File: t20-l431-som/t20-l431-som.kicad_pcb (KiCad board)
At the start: 4 copper layers, 10.1 x 12.2 mm, 54 parts, among them U1 STM32L431-WLCSP64, U2 T20W80, U3 MX25U3232F, U4 MODULE_INTERNAL_T20_L431_HOST, U5 LP3986TL-2518/NOPB, U6 74LVC1T45_DSBGA_YZP, U7 TPS22916BYFPR, U8 SIT8021AI-J4-XXS-16.000000, U9 NCP139AFCT120T2G

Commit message: Various layout fixes for DRC
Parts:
- moved R7 0.20 mm to (89.2, 73.1)
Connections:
- U4 pad D11: (no net) -> /1V8
- U4 pad E10: (no net) -> /1V8
- U4 pad E11: (no net) -> /GND
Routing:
- net /1V8: track 13.0 -> 13.9 mm
- net /FPGA IO/GPIOL_21_CTRL1_CDI5: vias 2 -> 1
- net /3V3: vias 20 -> 19

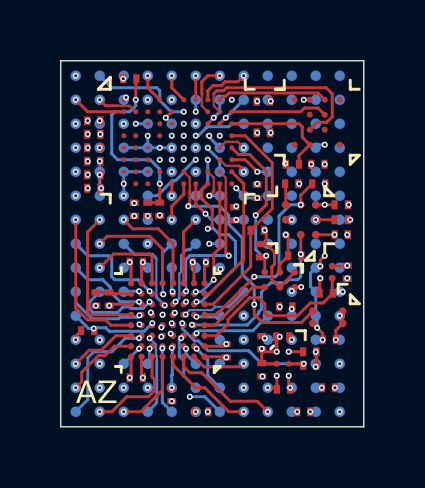
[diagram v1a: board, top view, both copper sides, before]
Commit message: T20/L431 SoM: added power/ground connections to all remaining NC lands
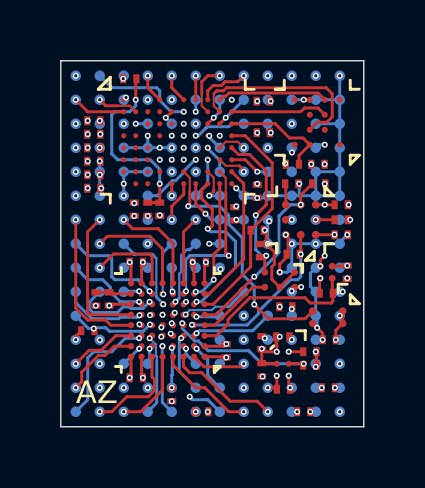
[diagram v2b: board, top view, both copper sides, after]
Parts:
- moved R2 0.07 mm to (90.3, 73.2)
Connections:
- U4 pad A10: (no net) -> /GND
- U4 pad A11: (no net) -> /GND
- U4 pad A12: (no net) -> /GND
- U4 pad A9: (no net) -> /GND
- U4 pad B10: (no net) -> /GND
- U4 pad B11: (no net) -> /GND
- U4 pad B12: (no net) -> /GND
- U4 pad C10: (no net) -> /3V3_FPGA
- U4 pad C11: (no net) -> /GND
- U4 pad C12: (no net) -> /GND
- U4 pad D10: (no net) -> /GND
- U4 pad D12: (no net) -> /GND
- U4 pad D9: (no net) -> /GND
- U4 pad E12: (no net) -> /GND
- U4 pad F10: (no net) -> /GND
- U4 pad F11: (no net) -> /GND
- U4 pad F12: (no net) -> /GND
- U4 pad F9: (no net) -> /GND
- U4 pad G9: (no net) -> /1V8
- U4 pad H10: (no net) -> /GND
- U4 pad H11: (no net) -> /GND
- U4 pad H12: (no net) -> /GND
- U4 pad H9: (no net) -> /1V8
- U4 pad J10: (no net) -> /GND
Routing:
- net /GND: track 84.0 -> 103.1 mm, vias 61 -> 70
- net /1V8: track 13.9 -> 14.9 mm, vias 7 -> 9
- net /3V3_FPGA: track 19.6 -> 19.9 mm, vias 10 -> 11

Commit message: Final design ready to order
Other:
- rule pad_to_mask_clearance: 0 -> 0.05
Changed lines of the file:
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@@
 			(dielectric_constraints no)
 		)
-		(pad_to_mask_clearance 0)
+		(pad_to_mask_clearance 0.05)
 		(allow_soldermask_bridges_in_footprints no)
 		(tenting front back)
@@
 	)
 	(segment
-		(start 83.67543 75.191423)
-		(end 84.493627 75.191423)
-		(width 0.1)
-		(layer "B.Cu")
-		(net 96)
-	)
-	(segment
-		(start 84.949999 75.059025)
-		(end 85.336235 75.059025)
-		(width 0.1)
-		(layer "B.Cu")
-		(net 96)
-	)
-	(segment
-		(start 84.493627 75.191423)
-		(end 84.676024 75.009026)
+		(start 83.543629 75.059622)
+		(end 83.543629 74.856371)
 		(width 0.1)
 		(layer "B.Cu")
@@
 	)
 	(segment
-		(start 83.543629 74.856371)
-		(end 83.543629 75.059622)
+		(start 85.336235 75.059025)
+		(end 84.626025 75.059025)
 		(width 0.1)
 		(layer "B.Cu")
@@
 	)
 	(segment
-		(start 84.9 75.009026)
-		(end 84.949999 75.059025)
+		(start 85.561233 74.834025)
+		(end 85.336235 75.059025)
 		(width 0.1)
 		(layer "B.Cu")
@@
 	)
 	(segment
-		(start 83.543629 75.059622)
+		(start 84.493627 75.191423)
 		(end 83.67543 75.191423)
 		(width 0.1)
@@
 	)
 	(segment
-		(start 85.336235 75.059025)
-		(end 85.561233 74.834025)
+		(start 84.626025 75.059025)
+		(end 84.493627 75.191423)
 		(width 0.1)
 		(layer "B.Cu")
@@
 	)
 	(segment
-		(start 84.676024 75.009026)
-		(end 84.9 75.009026)
+		(start 83.543629 74.856371)
+		(end 83.9 74.5)
 		(width 0.1)
 		(layer "B.Cu")
@@
 	)
 	(segment
-		(start 83.9 74.5)
-		(end 83.543629 74.856371)
+		(start 83.67543 75.191423)
+		(end 83.543629 75.059622)
 		(width 0.1)
 		(layer "B.Cu")

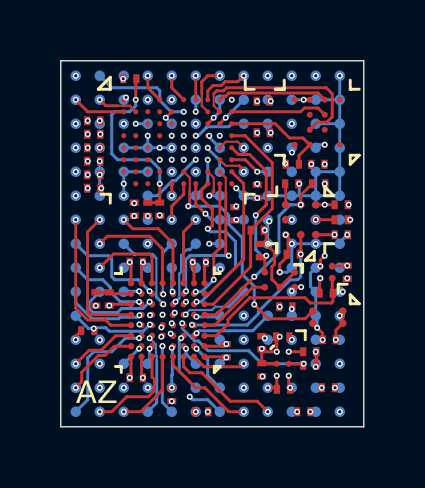
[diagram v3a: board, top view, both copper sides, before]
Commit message: Updated T20-L431 with HDI stackup and hopefully more JLC-friendly drills
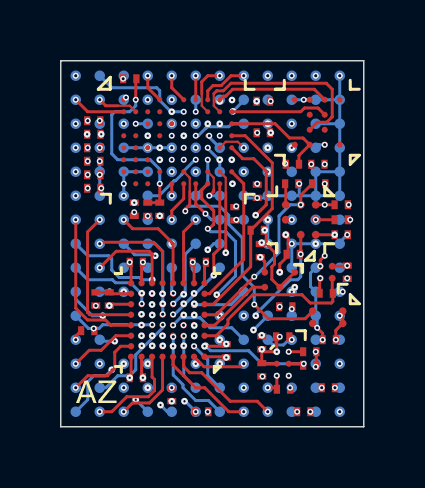
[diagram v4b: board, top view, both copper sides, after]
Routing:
- net /CROSS_SPI_CS_N: track 5.59 -> 4.80 mm
- net /PA2: track 3.04 -> 2.30 mm, vias 1 -> 3
- net /3V3: track 40.5 -> 41.3 mm, vias 19 -> 24
- net /1V8: track 14.9 -> 15.6 mm, vias 9 -> 12
- net /GND: track 103.1 -> 103.7 mm, vias 70 -> 81
- net /3V3_FPGA: track 19.9 -> 20.4 mm, vias 11 -> 12
- net /MCU_BOOT0: track 3.71 -> 3.21 mm, vias 2 -> 4
- net /PC5: track 2.73 -> 2.24 mm, vias 2 -> 1
- net /Power/1V2: track 24.9 -> 25.2 mm, vias 16 -> 17
- net /PB5: track 3.70 -> 3.45 mm, vias 2 -> 1
- net /PC15: track 4.06 -> 3.82 mm, vias 1 -> 3
- net /2V5_EN: track 5.93 -> 5.71 mm, vias 2 -> 4
- net /CROSS_SPI_MOSI: track 5.68 -> 5.89 mm, vias 2 -> 4
- net /PC8: track 3.20 -> 3.01 mm, vias 2 -> 3
- net /FPGA IO/GPIOL_46: track 0.57 -> 0.40 mm, vias 1 -> 3
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- added copper zone on In2.Cu, net /GND
